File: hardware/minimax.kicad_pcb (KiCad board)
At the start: 4 copper layers, 35 x 40 mm, 44 parts, among them J1 524352271, J2 2FA1-NZSP-PCBB6, J3 PRT-14417, J4 PRT-14417, U1 MAX96717GTJ/VY+, U2 MAX20049ATED/VY+

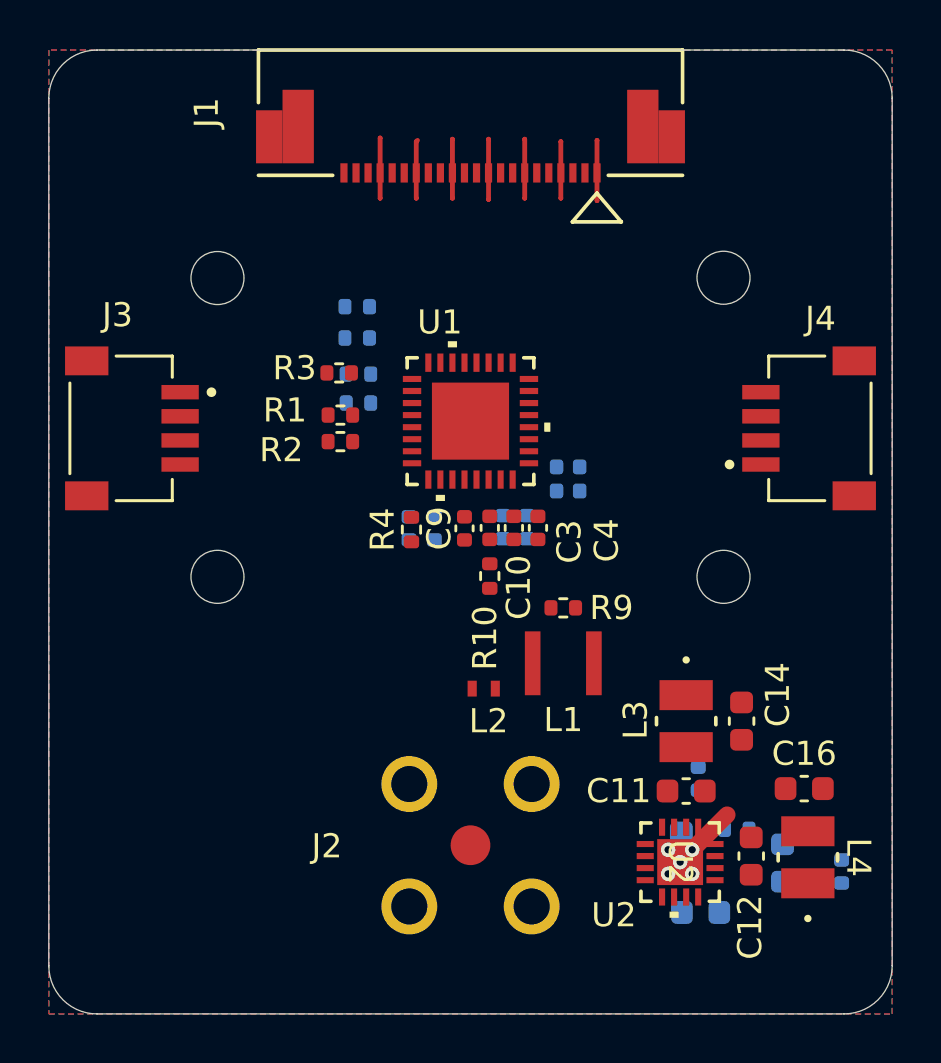
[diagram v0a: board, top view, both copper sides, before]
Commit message: cleaned up power supply and started minor power plane routing
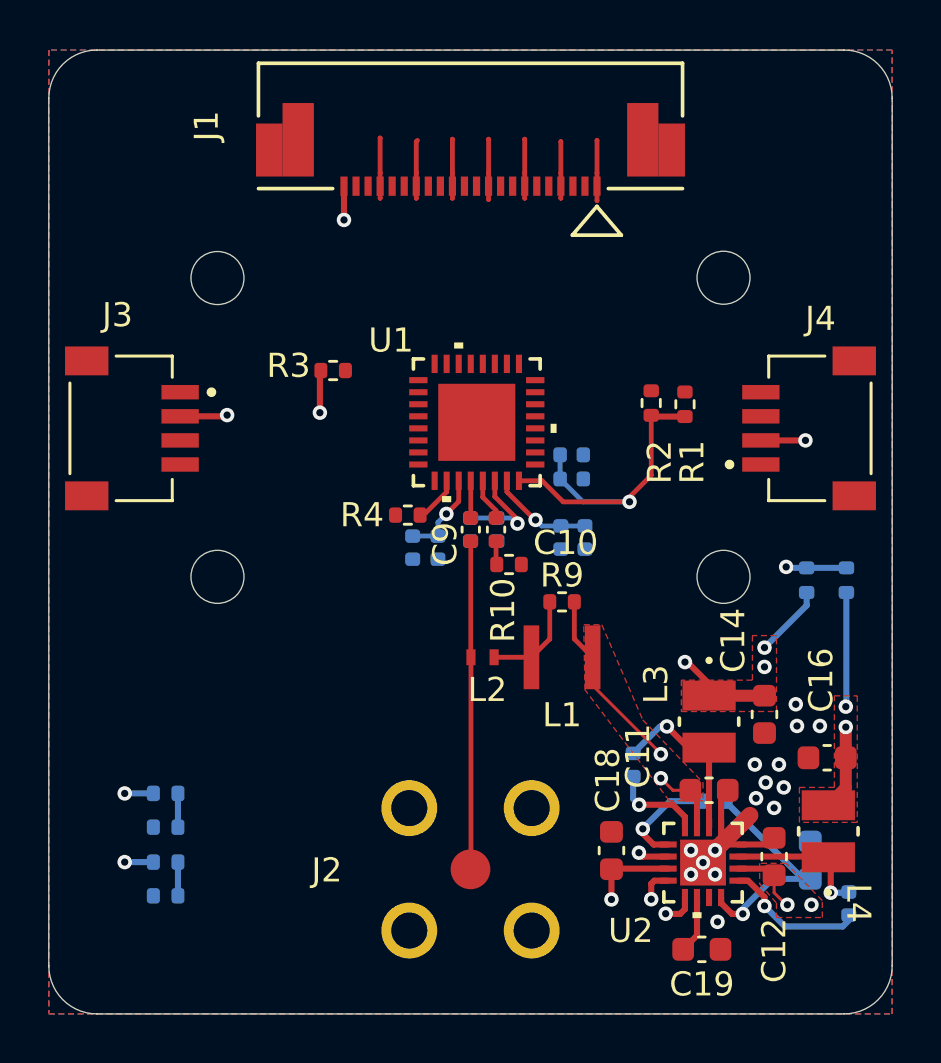
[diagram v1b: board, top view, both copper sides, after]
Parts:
- added R12: 0R, Resistor_SMD:R_0402_1005Metric, B.Cu at (165.6, 110.0)
- added R13: 0R, Resistor_SMD:R_0402_1005Metric, B.Cu at (163.9, 110.0)
- C18, C19: moved to F.Cu
- C3, C4: moved to B.Cu
- moved R8 23.1 mm to (137.3, 123.1)
- moved R7 21.8 mm to (137.3, 120.2)
- moved R5 21.7 mm to (137.3, 118.8)
- moved R6 20.7 mm to (137.3, 121.7)
- moved R1 14.3 mm to (158.9, 102.7), turned to 90 degrees
- moved R2 13.0 mm to (157.5, 102.7), turned to 90 degrees
- moved C18 2.90 mm to (155.8, 121.2)
- moved C4 2.80 mm to (150.0, 107.9)
- moved C13 2.76 mm to (156.8, 117.7)
- moved C5 2.44 mm to (153.8, 108.2)
- moved C6 2.44 mm to (154.8, 108.2)
- moved C16 1.59 mm to (164.8, 117.4)
- moved C19 1.53 mm to (159.6, 125.3)
- moved R11 1.51 mm to (160.1, 119.2)
- moved L4 1.37 mm to (164.8, 120.4)
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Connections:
- net +3.3V renamed +3V3
- C1 pad 1: VDD18 -> +1V8
- C2 pad 1: VDD18 -> +1V8
- C5 pad 1: VDD -> +1V2
- C6 pad 1: VDD -> +1V2
- U1 pad 11: VDD18 -> +1V8
- U1 pad 15: VDD -> +1V2
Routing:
- net +3V3: track 0.00 -> 79.1 mm, vias 0 -> 7
- net VDDIO: track 0.00 -> 65.5 mm, vias 0 -> 5
- net +1V8: track 0.00 -> 41.9 mm, vias 0 -> 5
- net +1V2: track 0.00 -> 25.1 mm, vias 0 -> 2
- net /connector/V_POC: track 0.00 -> 23.1 mm, vias 0 -> 4
- net Net-(C9-Pad2): track 0.00 -> 13.6 mm
- net Net-(U2-BIAS): track 0.00 -> 9.69 mm, vias 0 -> 1
- net Net-(U2-LX2): track 0.00 -> 7.30 mm, vias 0 -> 1
- net Net-(U2-LX1): track 0.00 -> 6.14 mm, vias 0 -> 1
- net Net-(U2-BST1): track 0.00 -> 5.93 mm, vias 0 -> 1
- net Net-(U2-PGOOD): track 0.00 -> 4.37 mm, vias 0 -> 1
- net Net-(U1-CAP_VDD): track 0.00 -> 4.21 mm, vias 0 -> 1
- net Net-(L1-Pad2): track 0.00 -> 4.16 mm
- net Net-(U2-BST2): track 0.00 -> 3.83 mm, vias 0 -> 1
- net GND: track 19.9 -> 23.2 mm, vias 5 -> 15
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- added copper zone on F.Cu, net +1V8
- added copper zone on F.Cu, net +3V3
- added copper zone on F.Cu, net /connector/V_POC
- added copper zone on In2.Cu, net /connector/V_POC
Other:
- board text added: "VDDIO 1V8- 3V3-"

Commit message: more serializer layout, waiting to do stackup analysis
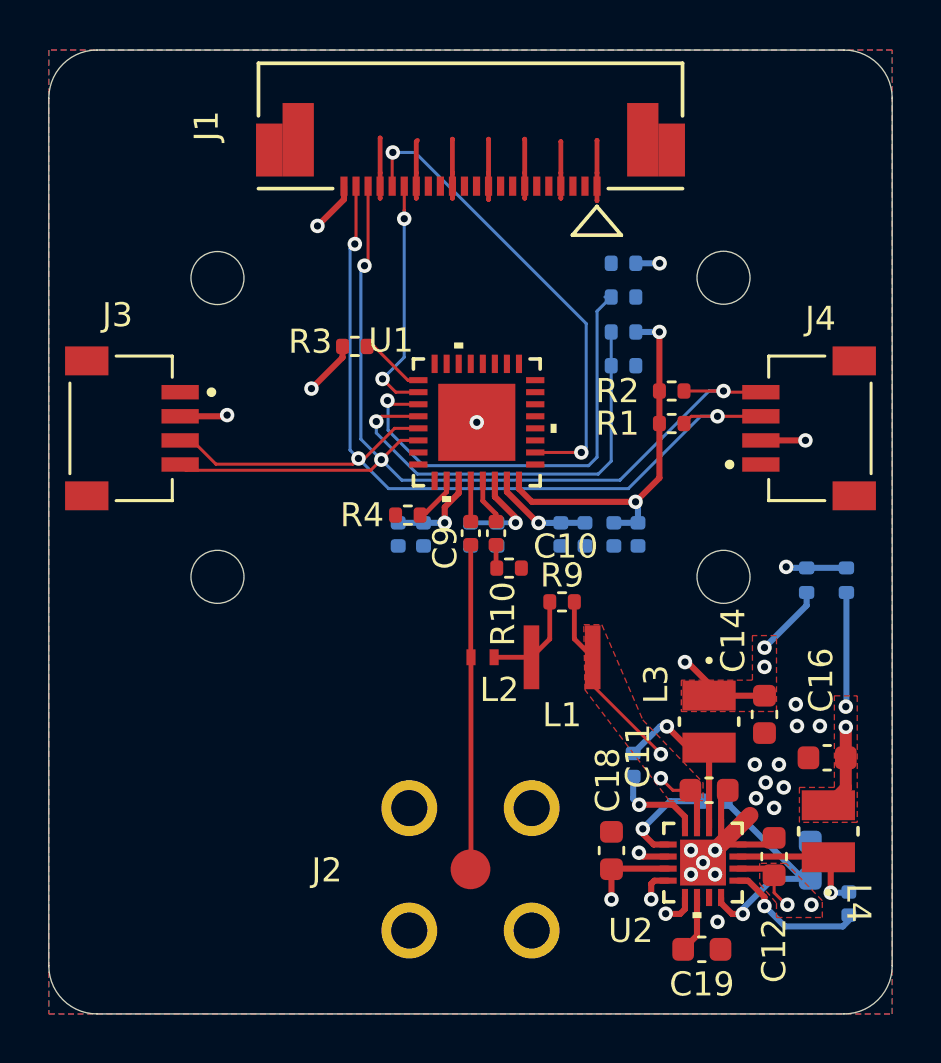
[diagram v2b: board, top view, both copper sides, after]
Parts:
- moved R5 29.1 mm to (156.3, 96.8), turned to 180 degrees
- moved R6 29.1 mm to (156.3, 99.7), turned to 180 degrees
- moved R7 29.1 mm to (156.3, 98.2), turned to 0 degrees
- moved R8 29.1 mm to (156.3, 101.1), turned to 0 degrees
- moved C7 4.30 mm to (156.9, 108.1), turned to -90 degrees
- moved C8 2.89 mm to (155.9, 108.1), turned to -90 degrees
- moved R3 1.35 mm to (145.2, 100.3)
- moved R2 0.99 mm to (158.3, 102.2), turned to 0 degrees
- moved R1 0.97 mm to (158.3, 103.5), turned to 0 degrees
- moved C1 0.81 mm to (147.0, 108.1)
- moved C2 0.81 mm to (148.1, 108.1)
- moved C3 0.20 mm to (151.1, 108.1)
- moved C4 0.20 mm to (150.0, 108.1)
- moved R10 0.15 mm to (151.6, 109.5)
- moved C10 0.15 mm to (151.1, 108.0)
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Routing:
- net /camera/MFP9_SDA: track 0.00 -> 42.4 mm, vias 0 -> 3
- net /camera/MFP10_SCL: track 0.00 -> 41.6 mm, vias 0 -> 3
- net /camera/LED_EN: track 0.00 -> 19.7 mm, vias 0 -> 2
- net MFP1_CFG0: track 1.40 -> 19.0 mm, vias 0 -> 1
- net MFP2_CFG1: track 1.40 -> 18.3 mm, vias 0 -> 1
- net VDDIO: track 65.5 -> 49.6 mm
- net /camera/POWER_EN: track 0.00 -> 10.1 mm, vias 0 -> 2
- net Net-(U1-PWDNB): track 0.00 -> 2.71 mm
- net GND: vias 15 -> 16
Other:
- board text added: "CFG0"
- board text added: "CFG1"

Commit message: clean up
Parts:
- J2: value 2FA1-NZSP-PCBB6 -> 59S1AC-40MT5-Z
- moved R5 20.7 mm to (136.6, 90.6)
- moved R6 20.7 mm to (136.6, 93.5)
- moved R7 20.7 mm to (136.6, 92.0)
- moved R8 20.7 mm to (136.6, 94.9)
- moved R2 16.7 mm to (142.6, 107.6), turned to 90 degrees
- moved R1 15.0 mm to (143.9, 107.6), turned to 90 degrees
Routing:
- net MFP1_CFG0: track 19.0 -> 1.47 mm
- net MFP2_CFG1: track 18.3 -> 1.83 mm
- net /camera/MIPI.CSI_D0_N: track 0.00 -> 12.6 mm, vias 0 -> 2
- net VDDIO: track 49.6 -> 37.3 mm, vias 5 -> 3
- net +3V3: track 78.6 -> 90.7 mm
- net /camera/MIPI.CSI_D1_N: track 0.00 -> 11.4 mm, vias 0 -> 2
- net /camera/MIPI.CSI_D0_P: track 0.00 -> 11.3 mm, vias 0 -> 2
- net /camera/MIPI.CSI_D1_P: track 0.00 -> 10.5 mm, vias 0 -> 2
- net /camera/LED_EN: track 19.7 -> 28.3 mm
- net MFP6: track 0.00 -> 1.94 mm, vias 0 -> 1
- net /camera/MFP10_SCL: track 41.6 -> 39.9 mm
- net /camera/MFP9_SDA: track 42.4 -> 41.0 mm
- net MFP5: track 0.00 -> 1.36 mm, vias 0 -> 1
- net /camera/MIPI.CSI_CLK_P: track 0.00 -> 0.64 mm
- net /camera/MIPI.CSI_CLK_N: track 0.00 -> 0.64 mm
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
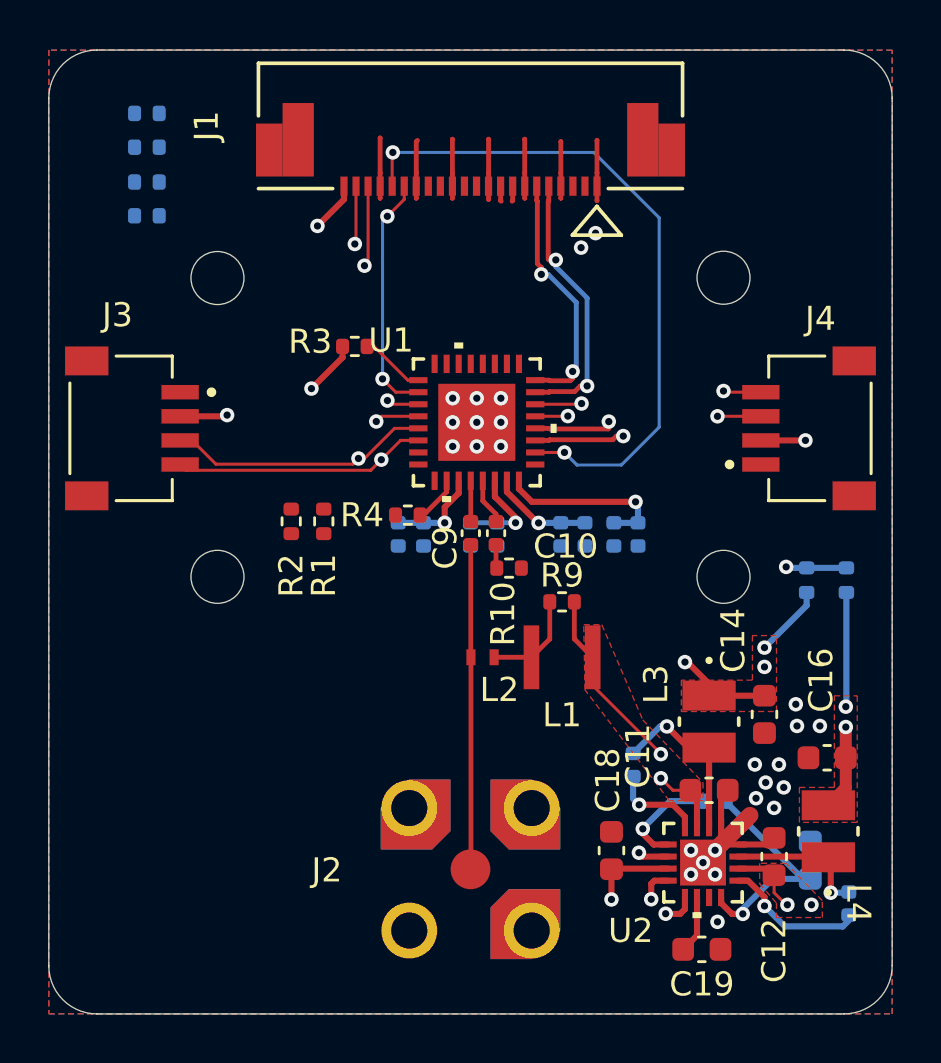
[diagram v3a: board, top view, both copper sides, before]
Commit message: added LED circuits and test points on extra MFPs
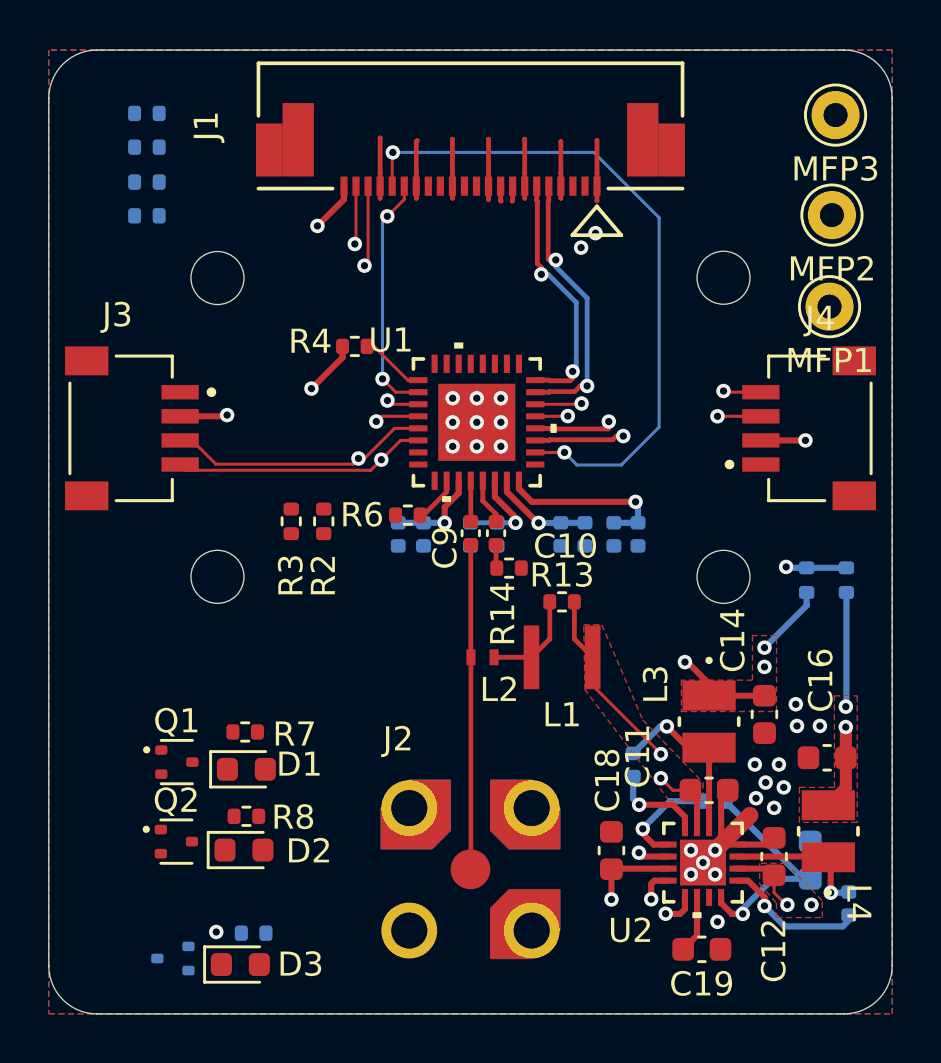
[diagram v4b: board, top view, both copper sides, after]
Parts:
- added D1: LED, LED_SMD:LED_0603_1608Metric, F.Cu at (140.7, 117.8)
- added D2: LED, LED_SMD:LED_0603_1608Metric, F.Cu at (140.6, 121.2)
- added D3: LED, LED_SMD:LED_0603_1608Metric, F.Cu at (140.4, 126.0)
- added MFP1: TestPoint, Connector_Pin:Pin_D1.0mm_L10.0mm, F.Cu at (164.9, 98.7)
- added MFP2: TestPoint, Connector_Pin:Pin_D1.0mm_L10.0mm, F.Cu at (165.0, 94.8)
- added MFP3: TestPoint, Connector_Pin:Pin_D1.0mm_L10.0mm, F.Cu at (165.2, 90.7)
- added Q1: DMG1012T, Package_TO_SOT_SMD:SOT-523, F.Cu at (137.8, 117.5)
- added Q2: DMG1012T, Package_TO_SOT_SMD:SOT-523, F.Cu at (137.8, 120.8)
- added Q3: DMG1012T, Package_TO_SOT_SMD:SOT-523, B.Cu at (137.7, 125.7)
- added R16: 402, Resistor_SMD:R_0402_1005Metric, B.Cu at (141.0, 124.7)
- added R7: 402, Resistor_SMD:R_0402_1005Metric, F.Cu at (140.7, 116.3)
- added R8: 402, Resistor_SMD:R_0402_1005Metric, F.Cu at (140.7, 119.8)
- renumbered R12 to R1, R6 to R10, R7 to R11, R8 to R12, R9 to R13, R10 to R14, R11 to R15, R1 to R2, R2 to R3, R3 to R4, R13 to R5, R4 to R6, R5 to R9
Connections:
- U1 pad 17: MFP3 -> /gmsl/ERRB
- U1 pad 18: /camera/LED_EN -> /gmsl/LOCK
- U1 pad 21: MFP5 -> /camera/LED_EN
- U1 pad 22: MFP6 -> Net-(U1-MFP6)
- U1 pad 31: MFP7 -> Net-(U1-MFP7)
- U1 pad 32: MFP8 -> Net-(U1-MFP8)
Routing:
- net Net-(U1-MFP6): track 0.00 -> 1.94 mm, vias 0 -> 1
- net MFP6: track 1.94 -> 0.00 mm, vias 1 -> 0
- net /camera/LED_EN: track 28.3 -> 29.6 mm, vias 2 -> 3
- net MFP5: track 1.36 -> 0.00 mm, vias 1 -> 0
- net GND: vias 24 -> 25

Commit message: cleaned up fakra footprint
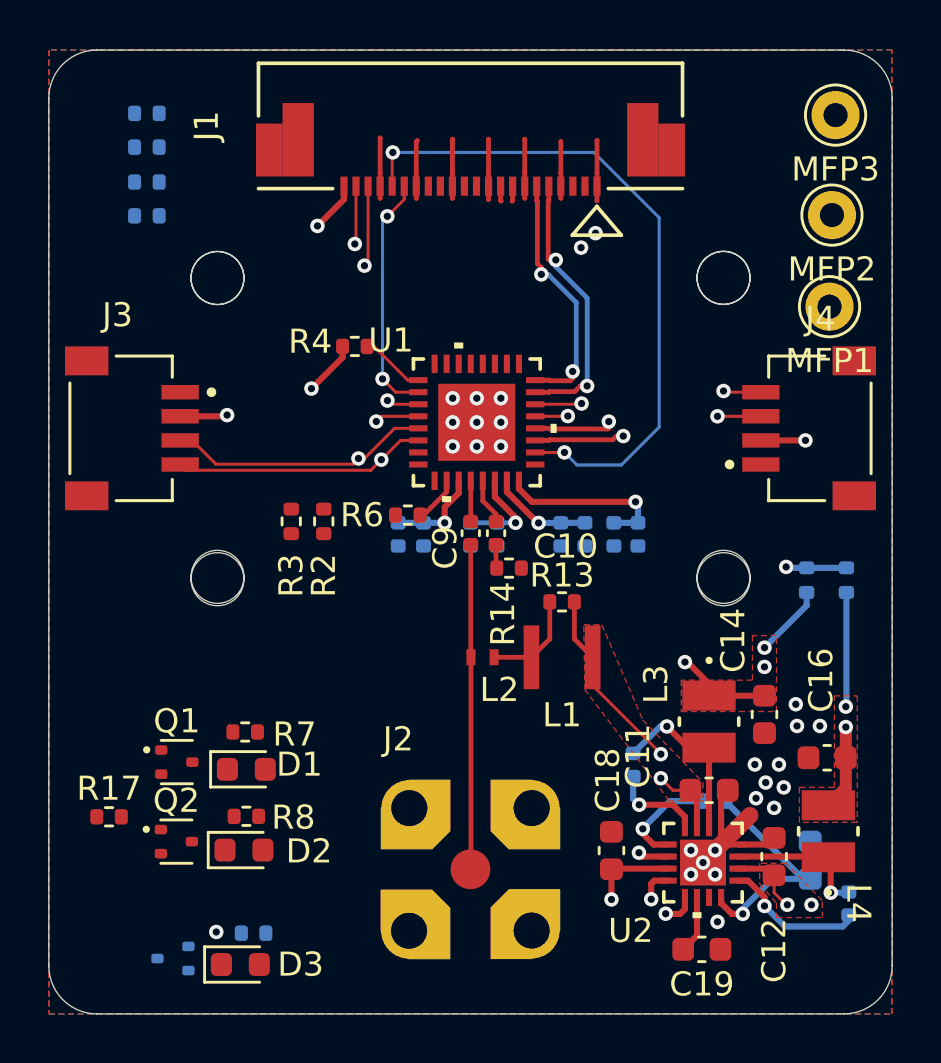
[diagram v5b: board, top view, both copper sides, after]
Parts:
- added R17: 5.1K, Resistor_SMD:R_0402_1005Metric, F.Cu at (135.0, 119.8)
- added REF**: RaspberryPiCameraV2, user:RaspberryPiCameraV2, B.Cu at (150.0, 95.5)
- R11, R2, R3, R4, R9: value 10K -> 5.1K
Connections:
- U1 pad 17: /gmsl/ERRB -> /gmsl/LOCK
- U1 pad 18: /gmsl/LOCK -> /gmsl/ERRB

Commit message: general layout changes
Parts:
- removed REF**: RaspberryPiCameraV2, user:RaspberryPiCameraV2
- Q3, R16: moved to F.Cu
- moved R17 26.7 mm to (157.6, 105.6), turned to 180 degrees
- moved R3 16.9 mm to (158.6, 102.1), turned to 0 degrees
- moved R2 15.3 mm to (158.6, 103.3), turned to 0 degrees
- moved Q3 3.58 mm to (140.0, 123.0)
- moved R16 3.42 mm to (138.0, 123.0), turned to -90 degrees
- moved Q1 3.36 mm to (140.0, 115.0), turned to 180 degrees
- moved R7 2.95 mm to (138.0, 115.0), turned to -90 degrees
- moved R11 2.88 mm to (136.8, 94.9)
- moved R9 2.88 mm to (136.8, 93.5)
- moved Q2 2.88 mm to (140.0, 119.0), turned to 180 degrees
- moved R8 2.82 mm to (138.0, 119.0), turned to -90 degrees
- moved R10 2.79 mm to (136.8, 90.7)
- moved R12 2.79 mm to (136.8, 92.1)
- moved D1 1.90 mm to (139.0, 117.0), turned to 180 degrees
- moved D3 1.73 mm to (139.0, 125.0), turned to 180 degrees
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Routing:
- net VDDIO: track 37.3 -> 65.1 mm, vias 3 -> 5
- net MFP2_CFG1: track 1.83 -> 21.4 mm
- net MFP1_CFG0: track 1.47 -> 17.3 mm
- net /camera/LED_EN: track 29.6 -> 18.9 mm, vias 3 -> 2
- net /camera/MIPI.CSI_D1_N: track 11.4 -> 3.37 mm, vias 2 -> 1
- net /camera/MIPI.CSI_D0_N: track 12.6 -> 5.64 mm
- net /camera/MIPI.CSI_D1_P: track 10.5 -> 3.74 mm, vias 2 -> 1
- net /camera/MIPI.CSI_D0_P: track 11.3 -> 5.29 mm
- net /gmsl/LOCK: track 0.00 -> 4.57 mm
- net Net-(U1-MFP6): track 1.94 -> 0.00 mm, vias 1 -> 0
- net /camera/MFP10_SCL: track 39.9 -> 41.3 mm
- net /gmsl/ERRB: track 0.00 -> 1.21 mm, vias 0 -> 1
- net /camera/MFP9_SDA: track 41.0 -> 42.2 mm
- net /camera/MIPI.CSI_D3_P: track 0.00 -> 1.10 mm
- net /camera/MIPI.CSI_D3_N: track 0.00 -> 1.10 mm
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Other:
- rule pad_to_mask_clearance: 0.0508 -> 0.0762

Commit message: finished schematics and layout, need final aesthetic touches
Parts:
- added R18: 5.1K, Resistor_SMD:R_0402_1005Metric, F.Cu at (156.7, 102.6)
- C3: footprint Capacitor_SMD:C_0402_1005Metric -> Capacitor_SMD:C_0603_1608Metric
- moved MFP1 1.00 mm to (165.0, 97.5)
- moved MFP2 0.85 mm to (165.0, 94.0)
- moved C3 0.63 mm to (150.9, 108.7)
- moved C4 0.57 mm to (149.6, 108.5)
- moved MFP3 0.25 mm to (165.0, 90.5)
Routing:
- net +3V3: track 90.7 -> 22.4 mm, vias 7 -> 10
- net /gmsl/LOCK: track 4.57 -> 34.0 mm, vias 0 -> 3
- net /gmsl/ERRB: track 1.21 -> 30.3 mm, vias 1 -> 3
- net Net-(U1-MFP7): track 0.00 -> 28.3 mm, vias 0 -> 1
- net Net-(U1-MFP8): track 0.00 -> 23.6 mm, vias 0 -> 1
- net Net-(Q3-G): track 4.37 -> 27.3 mm, vias 1 -> 2
- net Net-(U1-MFP6): track 0.00 -> 20.0 mm, vias 0 -> 1
- net /camera/MIPI.CSI_CLK_P: track 0.00 -> 13.6 mm
- net /camera/MIPI.CSI_CLK_N: track 0.00 -> 13.6 mm
- net /camera/MIPI.CSI_D2_N: track 0.00 -> 13.2 mm, vias 0 -> 2
- net /camera/MIPI.CSI_D2_P: track 0.00 -> 13.2 mm, vias 0 -> 2
- net /camera/MIPI.CSI_D3_P: track 1.10 -> 13.6 mm
- net /camera/MIPI.CSI_D3_N: track 1.10 -> 13.6 mm
- net /camera/POWER_EN: track 10.1 -> 21.4 mm
- net /camera/MIPI.CSI_D1_N: track 3.37 -> 13.5 mm, vias 1 -> 0
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- added copper zone on In2.Cu, net +3V3
- removed copper zone on In2.Cu, net GND
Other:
- board text added: "ERRB"
- board text added: "LOCK"
